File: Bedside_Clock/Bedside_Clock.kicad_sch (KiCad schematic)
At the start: 33 parts, among them J1 USBC_USB2.0, SW1 COLOR, SW2 MODE, SW3 BOOT, SW4 RESET, U1 ESP32-C3-MINI-1

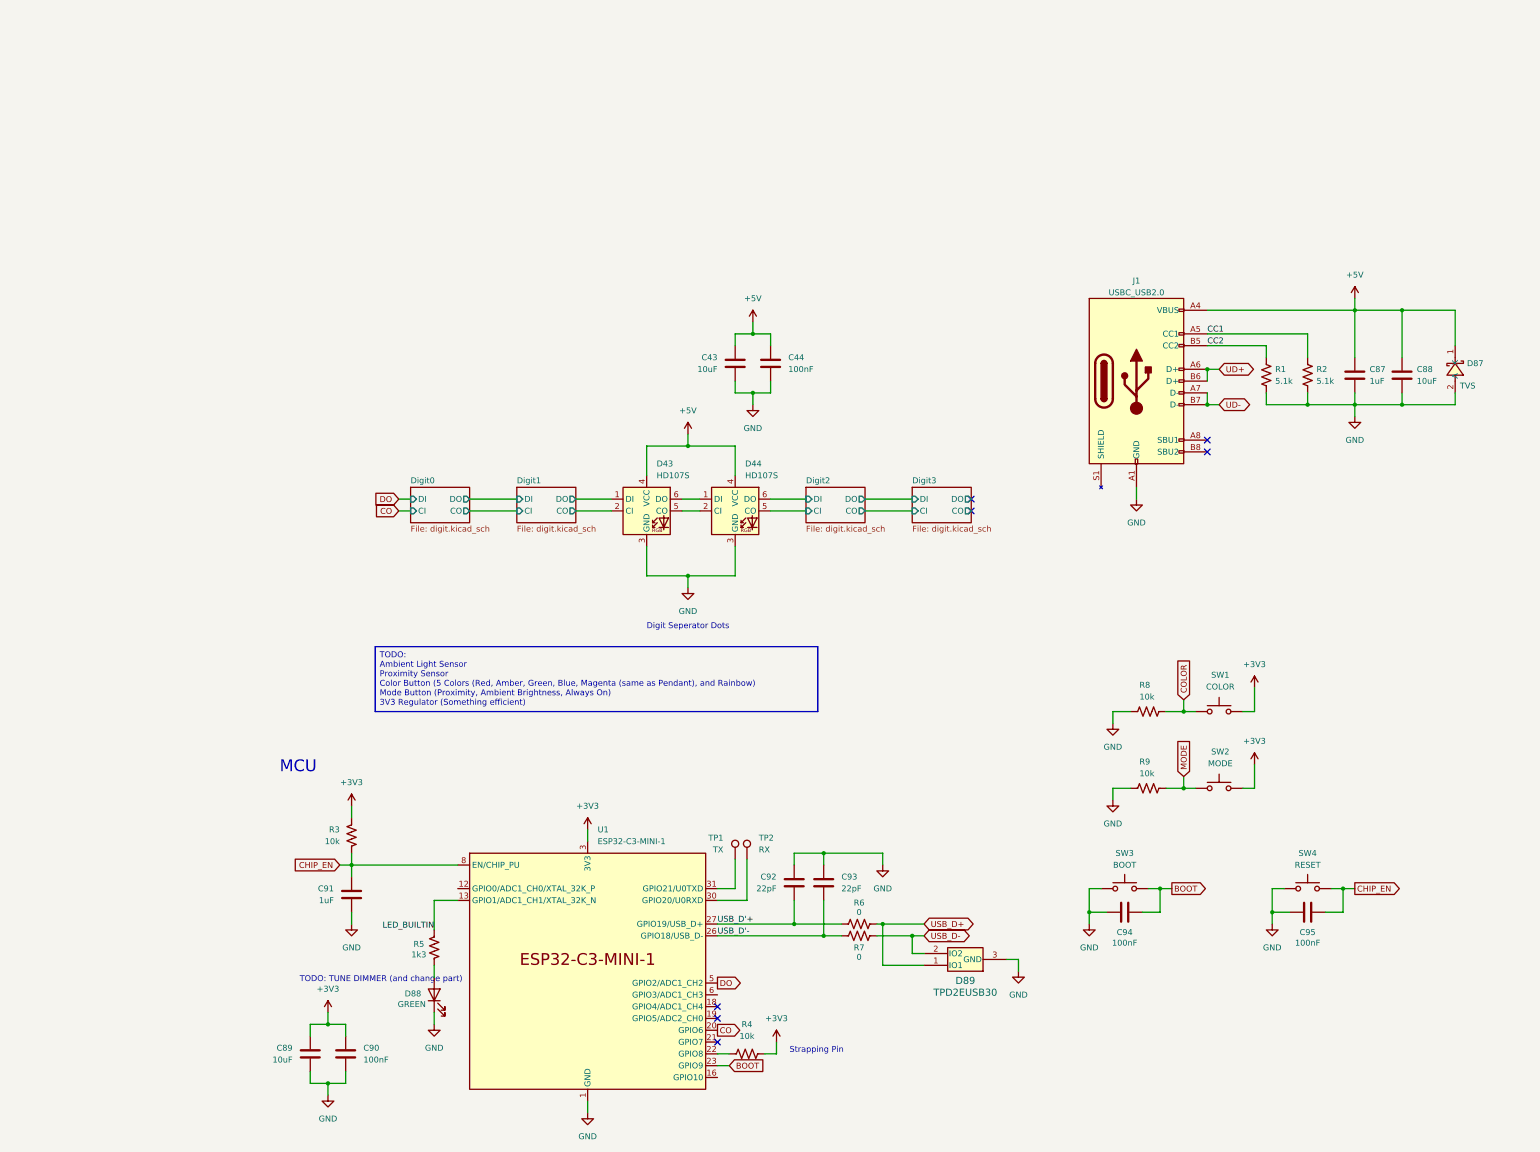
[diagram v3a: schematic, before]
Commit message: [HW] Routing progress Need to close on some parts
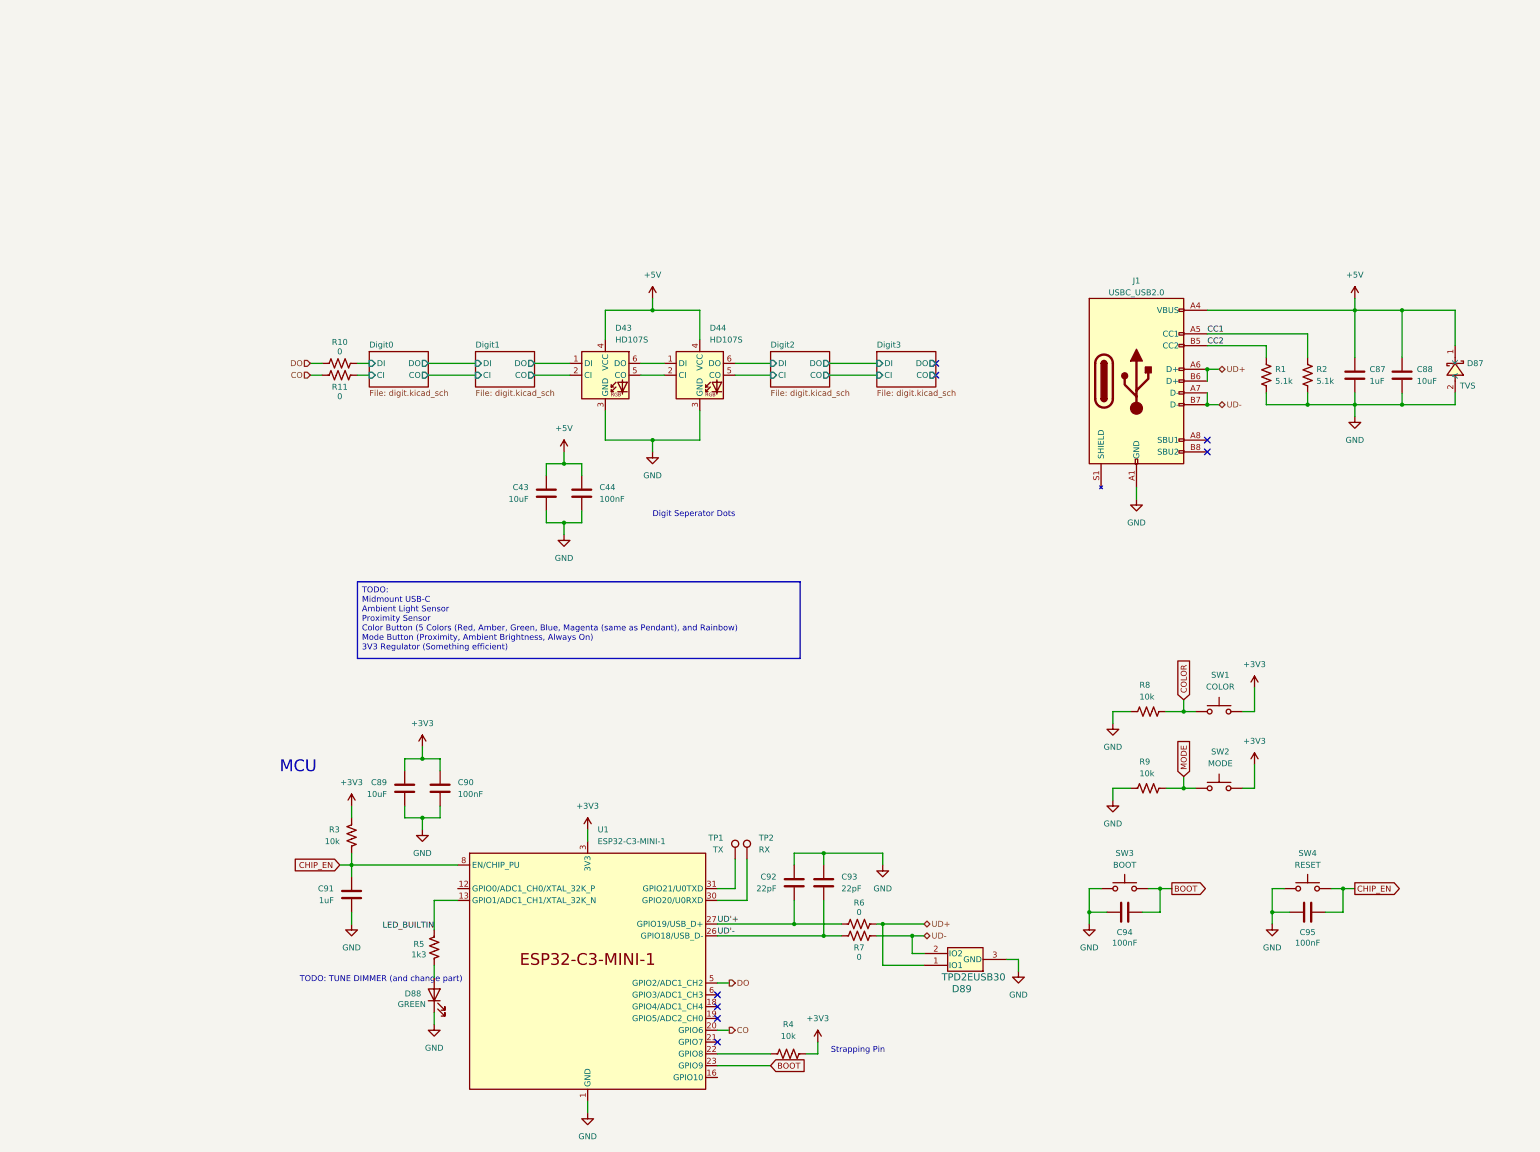
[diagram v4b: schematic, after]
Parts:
- added R10, R11: 0, Resistor_SMD:R_0603_1608Metric, symbol Device:R_US
- D89: footprint EasyEDA2KiCad:SOT-723_L1.2-W0.8-P0.80-LS1.2-BR -> TPD2EUSB30DRTR:DRT0003A; LCSC Part C5182099 -> (none)
- R3, R4, R5, R6, R7: footprint Resistor_SMD:R_0402_1005Metric -> Resistor_SMD:R_0603_1608Metric
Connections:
- net USB_D+ is gone; now on net UD+: D89.1 (IO1), R6.2
- net USB_D- is gone; now on net UD-: D89.2 (IO2), R7.2
- net CO: now also R11.1
- net DO: now also R10.1
- net at J1.S1 (SHIELD): now also J1.S2 (SHIELD), J1.S3 (SHIELD), J1.S4 (SHIELD)
- net USB_D'+ renamed UD'+
- net USB_D'- renamed UD'-
- new net Digit0/CI: R11.2
- new net Digit0/DI: R10.2
- no-connect marks 7 -> 8
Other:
- moved on the sheet: C43, C44, C89, C90, D43, D44, R4

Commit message: [HW] Switch to 4 layers and m mid mount USB-C
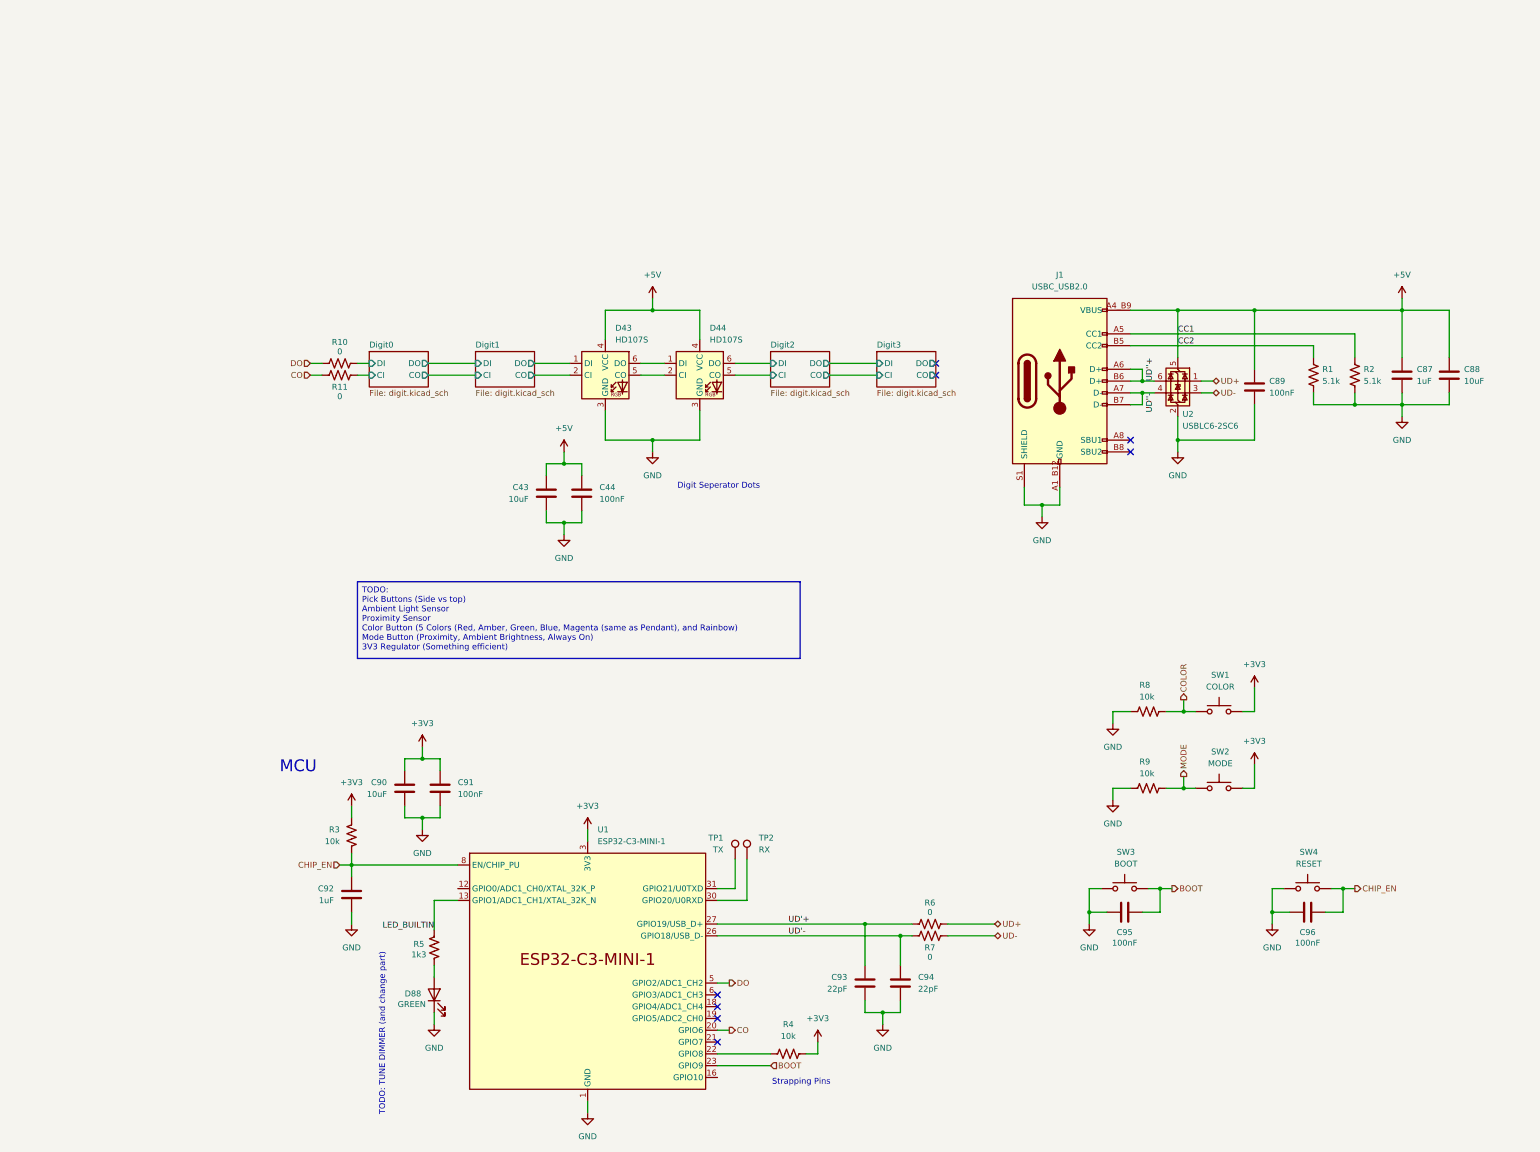
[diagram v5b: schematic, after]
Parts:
- removed D87: TVS, EasyEDA2KiCad:X2SON-2_L0.6-W0.3-P0.35_ESD441DPLR, symbol EasyEDA2KiCad:ESD441DPLR
- removed D89: TPD2EUSB30, TPD2EUSB30DRTR:DRT0003A, symbol TPD2EUSB30DRTR:TPD2EUSB30
- added C89: 100nF, Capacitor_SMD:C_0603_1608Metric, symbol Device:C
- added U2: USBLC6-2SC6, Package_TO_SOT_SMD:SOT-23-6, symbol Power_Protection:USBLC6-2SC6
- D88: footprint LED_SMD:LED_0603_1608Metric -> (none); LCSC Part C965806 -> (none)
- J1: footprint Connector_USB:USB_C_Receptacle_GCT_USB4085 -> USB4520_03_0_A:GCT_USB4520-03-0-A_REVA
- SW1, SW2: footprint EVQ_P7L01P:SW_EVQ-P7L01P -> (none)
- SW3, SW4: footprint EasyEDA2KiCad:KEY-SMD_L3.9-W3.0-LS5.0-EH -> (none); LCSC Part C18078117 -> (none)
- renumbered C89 to C90, C90 to C91, C91 to C92, C92 to C93, C93 to C94, C94 to C95, C95 to C96
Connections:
- net CC1 is gone; now on net +5V: J1.A5 (CC1), R2.2
- net CC2 is gone; now on net +5V: J1.B5 (CC2), R1.2
- net +5V: now also J1.A4_B9 (VBUS), J1.B4_A9 (VBUS), C89.1, U2.5 (VBUS); no longer J1.A4 (VBUS), J1.A9 (VBUS), J1.B4 (VBUS), J1.B9 (VBUS)
- net BOOT: now also SW3.1; no longer SW3.2
- net CHIP_EN: now also SW4.1; no longer SW4.2
- net GND: now also C93.2, C94.2, J1.A1_B12 (GND), J1.B1_A12 (GND), J1.S1 (SHIELD), J1.S2 (SHIELD), J1.S3 (SHIELD), J1.S4 (SHIELD), SW3.2, SW4.2, C89.2, U2.2 (GND); no longer C93.1, C94.1, J1.A1 (GND), J1.A12 (GND), J1.B1 (GND), J1.B12 (GND), SW3.1, SW4.1
- net UD'+: now also C93.1; no longer C93.2
- net UD'-: now also C94.1; no longer C94.2
- net UD+: now also U2.1 (I/O1); no longer J1.A6 (D+), J1.B6 (D+)
- net UD-: now also U2.3 (I/O2); no longer J1.A7 (D-), J1.B7 (D-)
- new net UD''+: J1.A6 (D+), J1.B6 (D+), U2.6 (I/O1)
- new net UD''-: J1.A7 (D-), J1.B7 (D-), U2.4 (I/O2)
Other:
- note added: "Strapping Pins"
- note removed: "Strapping Pin"
- moved on the sheet: C87, C88, C93, C94, R1, R2, R6, R7

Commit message: [HW] Clean up and layout improvements
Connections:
- net COLOR: now also U1.18 (GPIO4/ADC1_CH4)
- net MODE: now also U1.21 (GPIO7)
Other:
- moved on the sheet: C90, C91, C92, C93, C94, D88, R3, R4, R5, R6, R7, TP1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

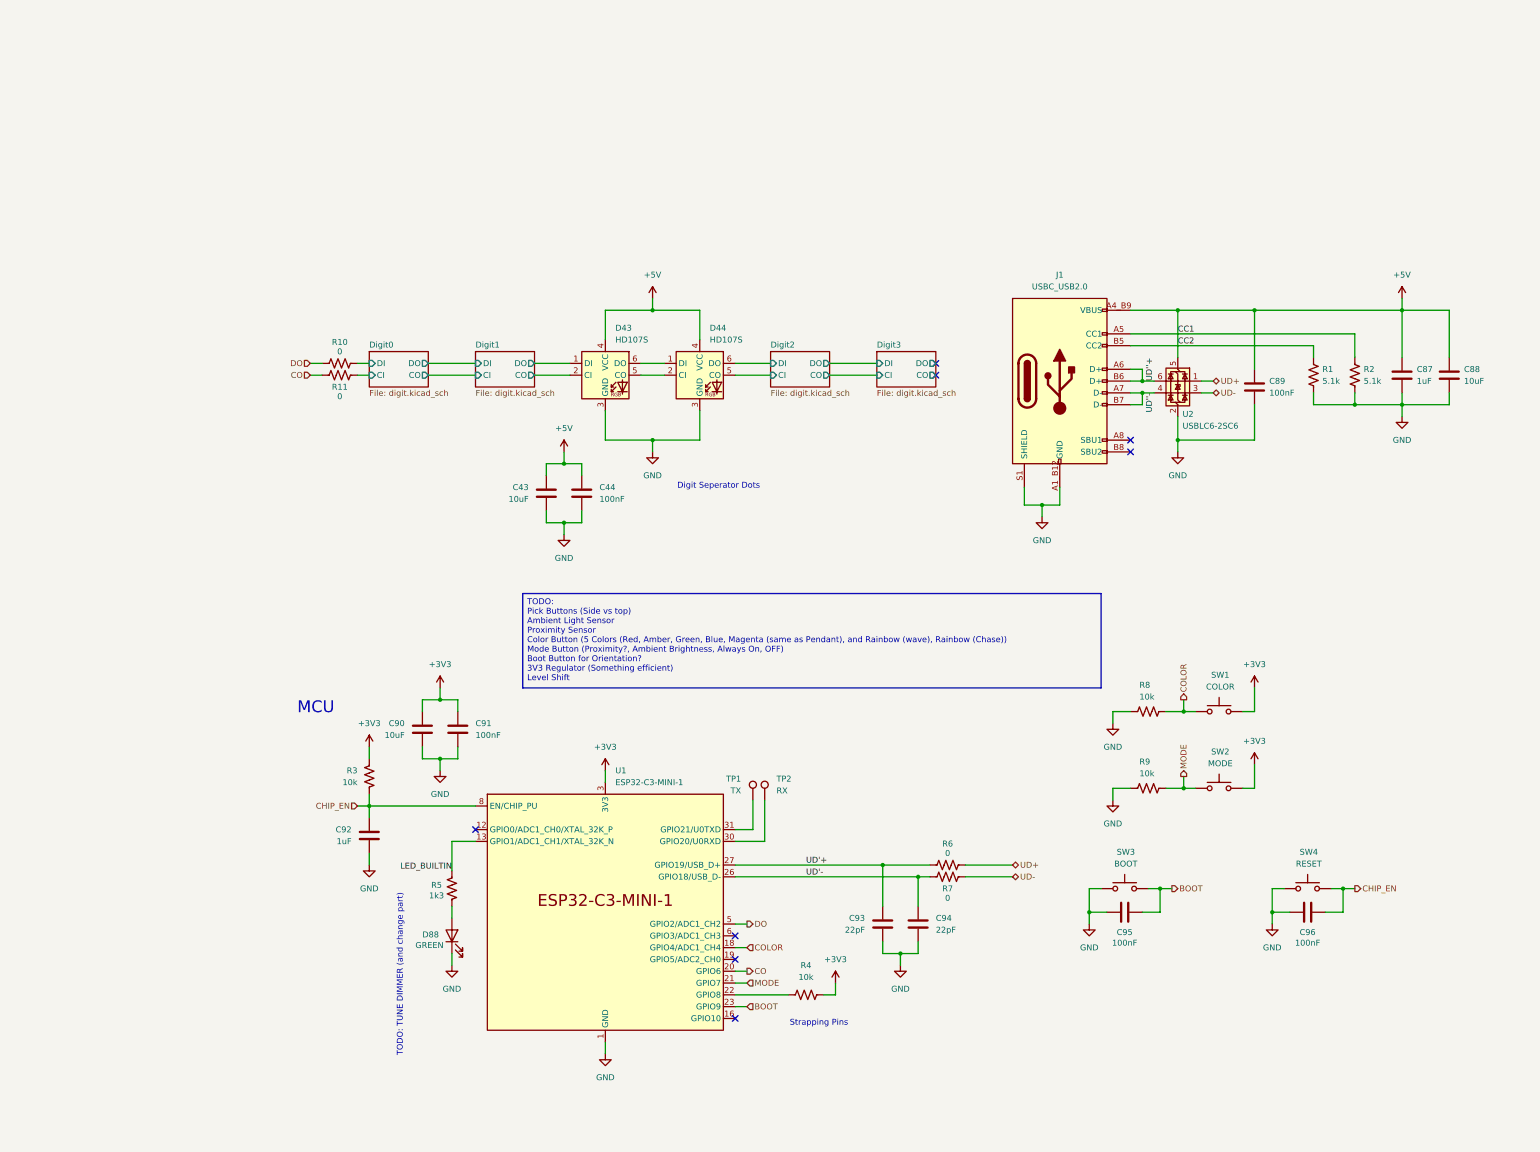
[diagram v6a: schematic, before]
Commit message: [HW] Add Ambient Light Sensor and Level Shifter
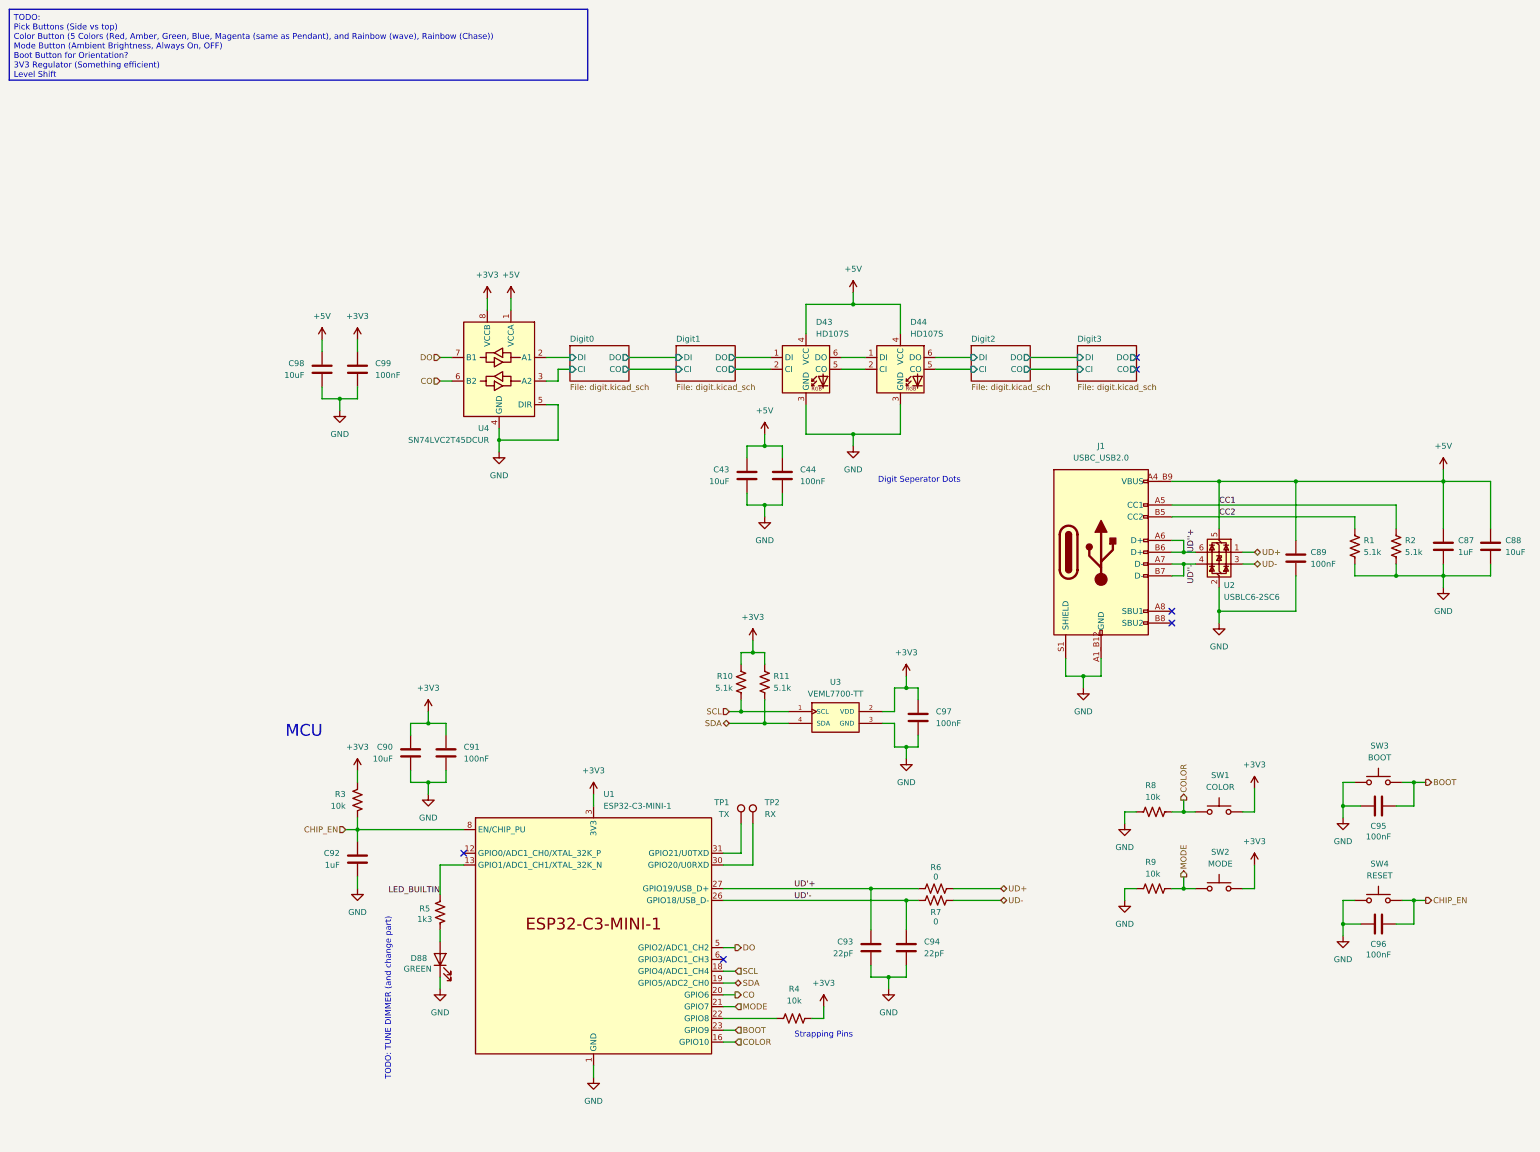
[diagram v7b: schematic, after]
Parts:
- added C97, C99: 100nF, Capacitor_SMD:C_0603_1608Metric, symbol Device:C
- added C98: 10uF, Capacitor_SMD:C_0603_1608Metric, symbol Device:C
- added U3: VEML7700-TT, VEML7700_TT:XDCR_VEML7700-TT, symbol VEML7700-TT:VEML7700-TT
- added U4: SN74LVC2T45DCUR, SN74LVC2T45DCTR:SOP65P400X130-8N, symbol Logic_LevelTranslator:SN74LVC2T45DCUR
- R10, R11: value 0 -> 5.1k; LCSC Part C17168 -> (none)
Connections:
- net +3V3: now also R10.2, R11.2, C97.1, C99.1, U3.2 (VDD), U4.8 (VCCB)
- net +5V: now also C98.1, U4.1 (VCCA)
- net CO: now also U4.6 (B2); no longer R11.1
- net COLOR: now also U1.16 (GPIO10); no longer U1.18 (GPIO4/ADC1_CH4)
- net DO: now also U4.7 (B1); no longer R10.1
- net Digit0/CI: now also U4.3 (A2); no longer R11.2
- net Digit0/DI: now also U4.2 (A1); no longer R10.2
- net GND: now also C97.2, C98.2, C99.2, U3.3 (GND), U4.4 (GND), U4.5 (DIR)
- net SDA: now reaches U1.19 (GPIO5/ADC2_CH0)
- net SDA: now also R11.1, U3.4 (SDA)
- new net SCL: R10.1, U1.18 (GPIO4/ADC1_CH4), U3.1 (SCL)
- no-connect marks 8 -> 6
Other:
- moved on the sheet: C43, C44, C87, C88, C89, C90, C91, C92, C93, C94, C95, C96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
